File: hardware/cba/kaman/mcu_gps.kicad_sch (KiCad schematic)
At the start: 40 parts, among them Q1 MMDT5551, Q2 DTC143X, Q3 DTC143X, SW1 SW_Push, SW2 SW_Push, U1 ESP32-C6-MINI-1, U2 L80-R, U3 NEO-M8N, U4 AT24CS64-SSHM

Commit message: hw(pcb): unorganized overlay 0.1v pcb
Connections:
- net GPS RX: now also U1.12 (IO0)
- net GPS TX: now also U1.13 (IO1)
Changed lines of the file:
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@@
+	(wire
+		(pts
+			(xy 31.75 82.55) (xy 36.83 82.55)
+		)
+		(stroke
+			(width 0)
+			(type default)
+		)
+	)
 	(wire
 		(pts
@@
 		(pts
 			(xy 144.78 27.94) (xy 157.48 27.94)
+		)
+		(stroke
+			(width 0)
+			(type default)
+		)
+	)
+	(wire
+		(pts
+			(xy 31.75 85.09) (xy 36.83 85.09)
 		)
 		(stroke
@@
 		)
 	)
+	(global_label "GPS RX"
+		(shape input)
+		(at 31.75 82.55 180)
+		(fields_autoplaced yes)
+		(effects
+			(font
+				(size 1.27 1.27)
+			)
+			(justify right)
+		)
+		(property "Intersheetrefs" "${INTERSHEET_REFS}"
+			(at 21.5682 82.55 0)
+			(hide yes)
+			(show_name no)
+			(do_not_autoplace no)
+			(effects
+				(font
+					(size 1.27 1.27)
+				)
+				(justify right)
+			)
+		)
+	)
 	(global_label "UART RX"
 		(shape input)
@@
 			(hide yes)
 			(show_name no)
+			(do_not_autoplace no)
+			(effects
+				(font
+					(size 1.27 1.27)
+				)
+				(justify right)
+			)
+		)
+	)
+	(global_label "GPS TX"
+		(shape output)
+		(at 31.75 85.09 180)
+		(fields_autoplaced yes)
+		(effects
+			(font
+				(size 1.27 1.27)
+			)
+			(justify right)
+		)
+		(property "Intersheetrefs" "${INTERSHEET_REFS}"
+			(at 21.8706 85.09 0)
+			(hide yes)
+			(show_name no)

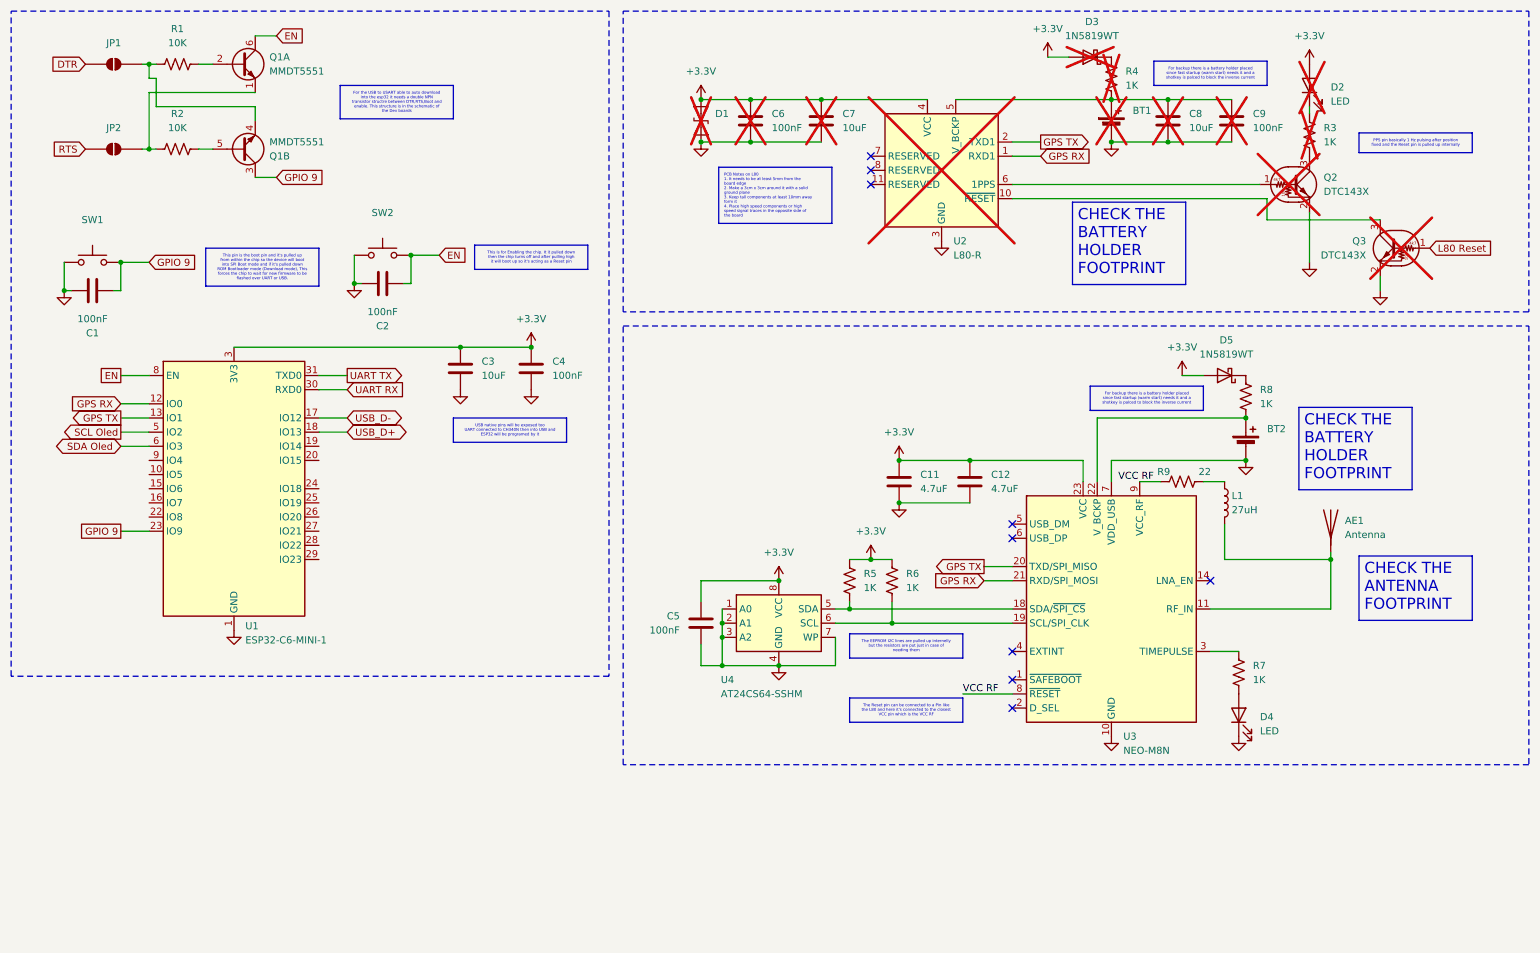
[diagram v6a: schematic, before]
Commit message: hw(schmatic): add ra-01 LoRa module
The second rf solution is done by ra-01 and the circuit needed to work
was pulled from datasheet and for antenna connector an SMA type is used
and there is a UFL on the module too
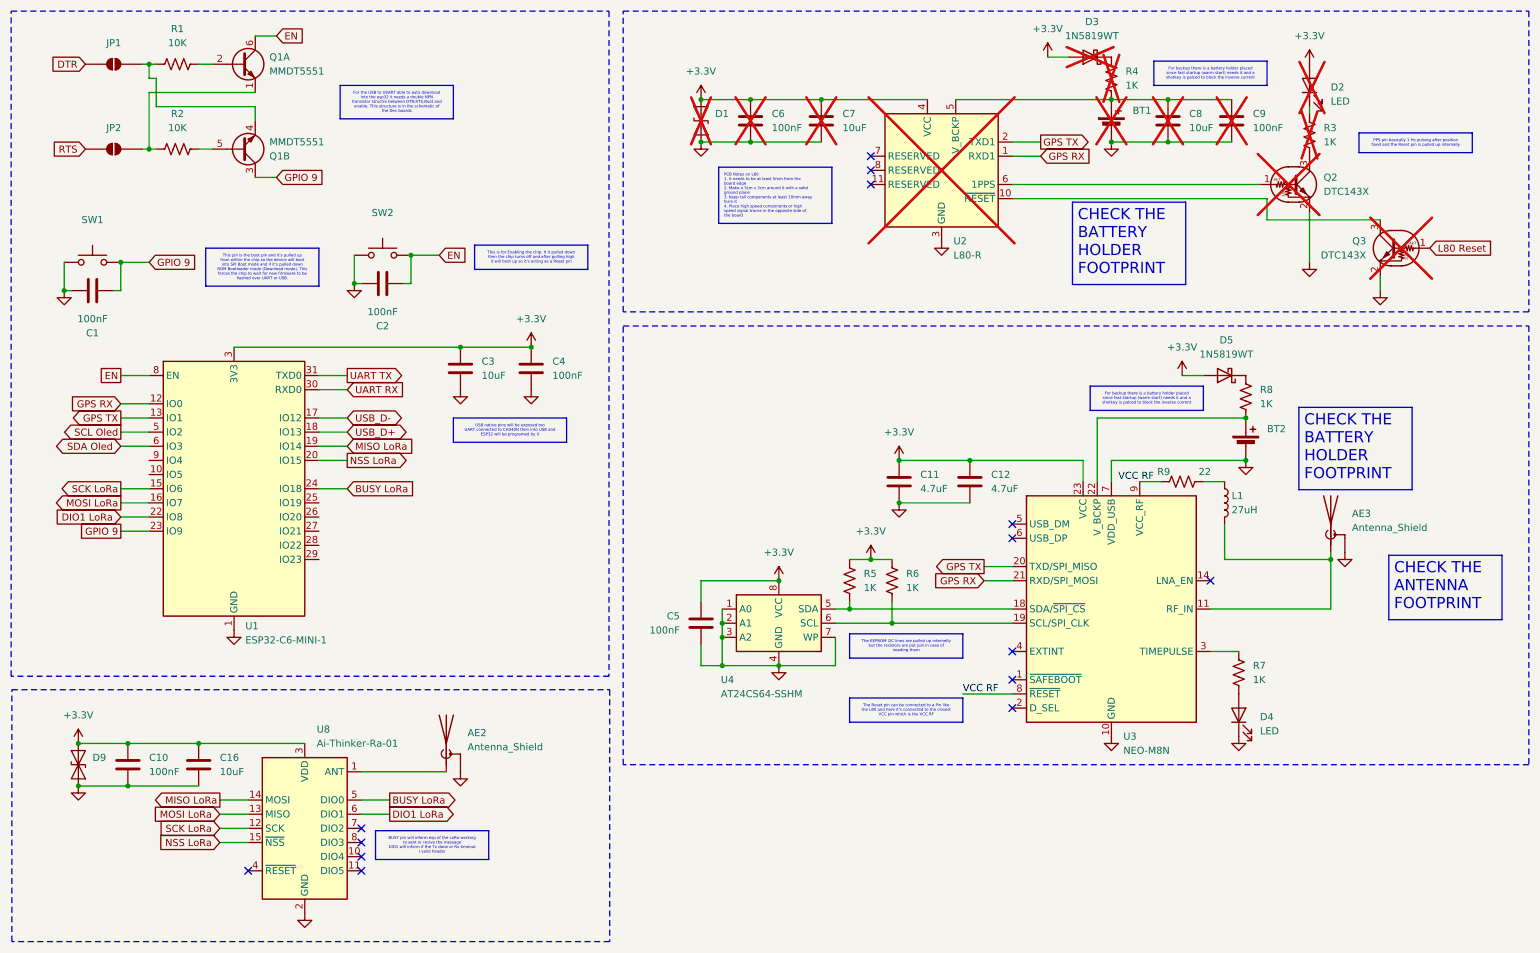
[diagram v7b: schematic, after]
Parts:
- removed AE1: Antenna, Connector_Coaxial:U.FL_Hirose_U.FL-R-SMT-1_Vertical, symbol Device:Antenna
- added AE2: Antenna_Shield, Connector_Coaxial:SMA_Amphenol_132134-11_Vertical, symbol Device:Antenna_Shield
- added AE3: Antenna_Shield, Connector_Coaxial:U.FL_Hirose_U.FL-R-SMT-1_Vertical, symbol Device:Antenna_Shield
- added C10: 100nF, Capacitor_SMD:C_0603_1608Metric_Pad1.08x0.95mm_HandSolder, symbol Device:C
- added C16: 10uF, Capacitor_SMD:C_0805_2012Metric_Pad1.18x1.45mm_HandSolder, symbol Device:C
- added D9: SD03C-MMD, Diode_SMD:D_SOD-323, symbol Diode:SD05C-01F
- added U8: Ai-Thinker-Ra-01, RF_Module:Ai-Thinker-Ra-01-LoRa, symbol RF_Module:Ai-Thinker-Ra-01
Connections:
- net +3.3V: now also C10.1, C16.1, D9.2 (A2), U8.3 (VDD)
- net GND: now also AE2.2 (Shield), AE3.2 (Shield), C10.2, C16.2, D9.1 (A1), U8.16 (GND), U8.2 (GND), U8.9 (GND)
- net SCK LoRa: now reaches U1.15 (IO6)
- net SCK LoRa: now also U8.12 (SCK)
- net MOSI LoRa: now reaches U1.16 (IO7)
- net MOSI LoRa: now also U8.13 (MISO)
- net MISO LoRa: now reaches U1.19 (IO14)
- net MISO LoRa: now also U8.14 (MOSI)
- net NSS LoRa: now reaches U1.20 (IO15)
- net NSS LoRa: now also U8.15 (~{NSS})
- net DIO1 LoRa: now reaches U1.22 (IO8)
- net DIO1 LoRa: now also U8.6 (DIO1)
- net BUSY LoRa: now reaches U1.24 (IO18)
- net BUSY LoRa: now also U8.5 (DIO0)
- net at L1.2, U3.11 (RF_IN): now also AE3.1 (A)
- new net: AE2.1 (A), U8.1 (ANT)
- no-connect marks 9 -> 14

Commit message: hw(pcb): final 0.2v pcb
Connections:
- net BUSY LoRa: now also U1.22 (IO8); no longer U1.24 (IO18)
- net DIO1 LoRa: now also U1.24 (IO18); no longer U1.22 (IO8)
- net MISO LoRa: now also U1.16 (IO7); no longer U1.19 (IO14)
- net MOSI LoRa: now also U1.19 (IO14); no longer U1.16 (IO7)
- net NSS LoRa: now also U1.15 (IO6); no longer U1.20 (IO15)
- net SCK LoRa: now also U1.20 (IO15); no longer U1.15 (IO6)
